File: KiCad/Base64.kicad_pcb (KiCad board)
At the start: 4 copper layers, 25.1 x 81.8 mm, 29 parts, among them J1 1473149-1, J2 Conn_01x03, U1 501MLFT, U10 68000_PinHeader, U2 SN74CBTD3861DGVR, U3 SN74CBTD3861DGVR, U4 SN74CBTD3861DGVR, U5 SN74CBTD3861DGVR, U6 SN74CBTD3861DGVR, U7 SN74CBTD3861DGVR, U8 SN74CBTD3861DGVR, U9 74AHCT1G17

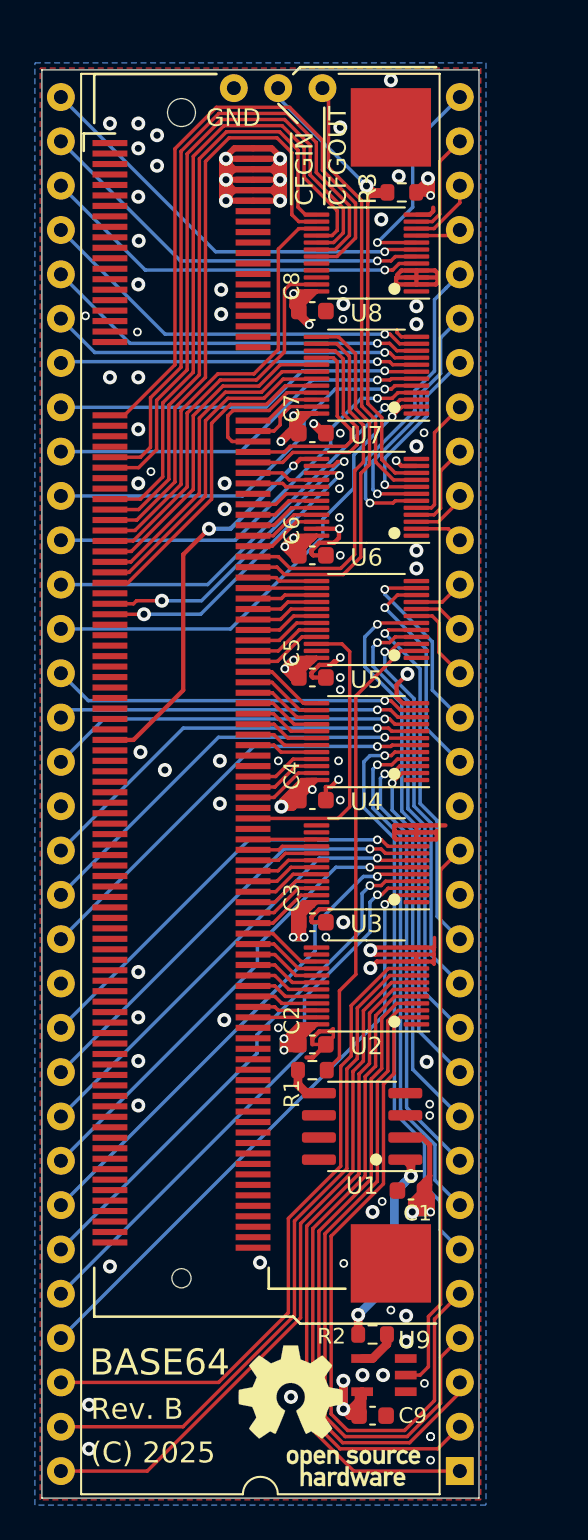
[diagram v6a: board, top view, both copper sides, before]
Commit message: Small silkscreen fixes and routing/VCC/GND-stitching improvements, better positioning of CFG-header
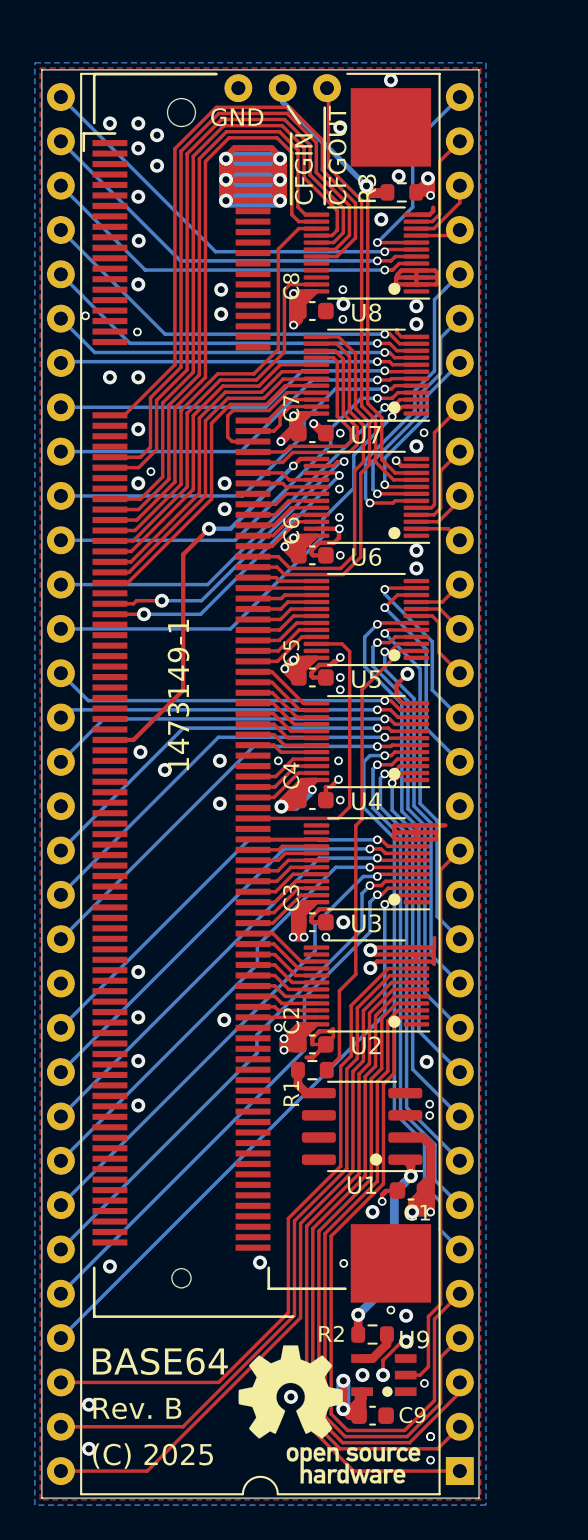
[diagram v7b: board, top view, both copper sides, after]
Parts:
- moved J2 0.26 mm to (105.7, 44.5)
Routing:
- net VCC: track 136.6 -> 160.9 mm
- net GND: track 57.9 -> 63.2 mm
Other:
- board text added: "1473149-1"

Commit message: Add a GND via
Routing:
- net GND: vias 80 -> 81
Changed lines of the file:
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@@
     (thickness 1.6)
     (drawings 19)
-    (tracks 1255)
+    (tracks 1256)
     (zones 0)
     (modules 29)
@@
   )
   (setup
-    (last_trace_width 0.5)
+    (last_trace_width 0.1524)
     (user_trace_width 0.2)
     (user_trace_width 0.25)
@@
     (fp_line (start -0.75 1.45) (end -0.75 -1.45) (layer F.Fab) (width 0.1))
     (fp_line (start -0.75 -0.5) (end 0.2 -1.45) (layer F.Fab) (width 0.1))
+    (fp_circle (center -0.2 -0.95) (end 0 -0.95) (layer F.SilkS) (width 0.2))
+    (fp_circle (center -0.2 -0.95) (end -0.15 -0.95) (layer F.SilkS) (width 0.12))
     (fp_text user %R (at 0 0) (layer F.Fab) hide
       (effects (font (size 1.27 1.27) (thickness 0.254)))
     )
-    (fp_circle (center -0.2 -0.95) (end 0 -0.95) (layer F.SilkS) (width 0.2))
-    (fp_circle (center -0.2 -0.95) (end -0.15 -0.95) (layer F.SilkS) (width 0.12))
     (pad 5 smd rect (at 1.25 -0.95 270) (size 0.5 1.25) (layers F.Cu F.Paste F.Mask)
       (net 2 VCC))
@@
   (segment (start 109.98212 116.325) (end 110.225 116.325) (width 0.2) (layer F.Cu) (net 1))
   (segment (start 108.9 117.40712) (end 109.98212 116.325) (width 0.2) (layer F.Cu) (net 1))
+  (via (at 91.85 74.35) (size 0.5) (drill 0.3) (layers F.Cu B.Cu) (net 1))
   (via (at 111.625 50.65) (size 0.5) (drill 0.3) (layers F.Cu B.Cu) (net 2))
   (via (at 111.475 49.675) (size 0.8) (drill 0.4) (layers F.Cu B.Cu) (net 2))
